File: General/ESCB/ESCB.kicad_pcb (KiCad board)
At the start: 2 copper layers, 35.8 x 17.5 mm, 3 parts, among them J1 Power_Signal, J2 Motor, U1 BESC

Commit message: Update ESCB.kicad_pcb
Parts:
- added G***: LOGO, extraparts:auv_logo, F.Cu at (159.5, 105.8)
- moved J1 21.1 mm to (172.2, 101.2)
- moved U1 21.0 mm to (162.8, 101.2)
- moved J2 20.7 mm to (150.2, 101.2)
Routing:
- net VCC: track 2.54 -> 0.00 mm, vias 10 -> 12
- net Net-(J1-Pad3): track 7.61 -> 8.96 mm
- net Net-(J2-Pad3): vias 3 -> 8
- net Net-(J2-Pad2): vias 3 -> 8
- net Net-(J2-Pad1): vias 3 -> 8
- net GND: vias 10 -> 12
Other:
- board text added: "BESC by Dang Le"
- board text removed: "BESC"

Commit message: Update ESCB.kicad_pcb
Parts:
- moved G*** 1.77 mm to (161.2, 105.5)
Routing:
- net VCC: vias 12 -> 31
- net Net-(J2-Pad3): vias 8 -> 17
- net Net-(J2-Pad2): vias 8 -> 10
- net Net-(J2-Pad1): vias 8 -> 17
- net GND: vias 12 -> 27
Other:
- board size 35.8 x 17.5 mm -> 36 x 17.6 mm

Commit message: Update ESCB.kicad_pcb
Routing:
- net Net-(J1-Pad3): track 8.96 -> 7.97 mm
- net VCC: vias 31 -> 66
- net Net-(J2-Pad3): vias 17 -> 21
- net Net-(J2-Pad1): vias 17 -> 21
- net GND: vias 27 -> 61

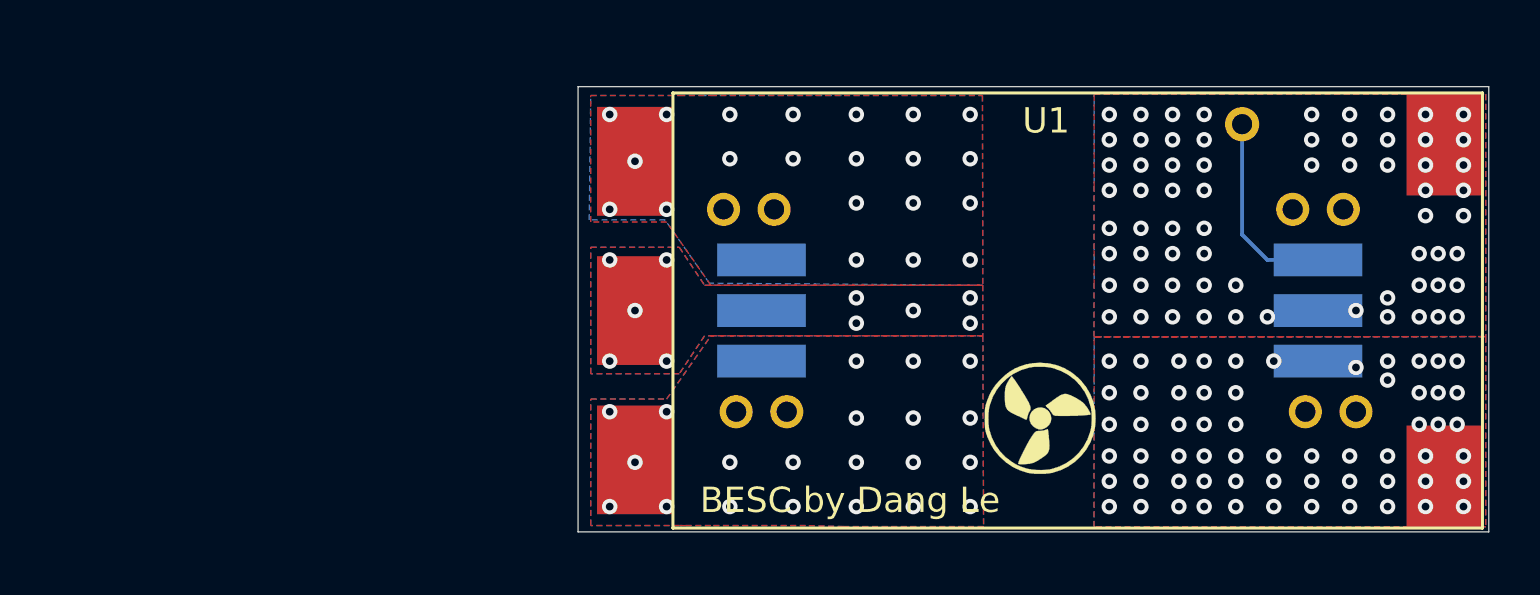
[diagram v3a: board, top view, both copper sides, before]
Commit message: Update Vua and Pore Clearance
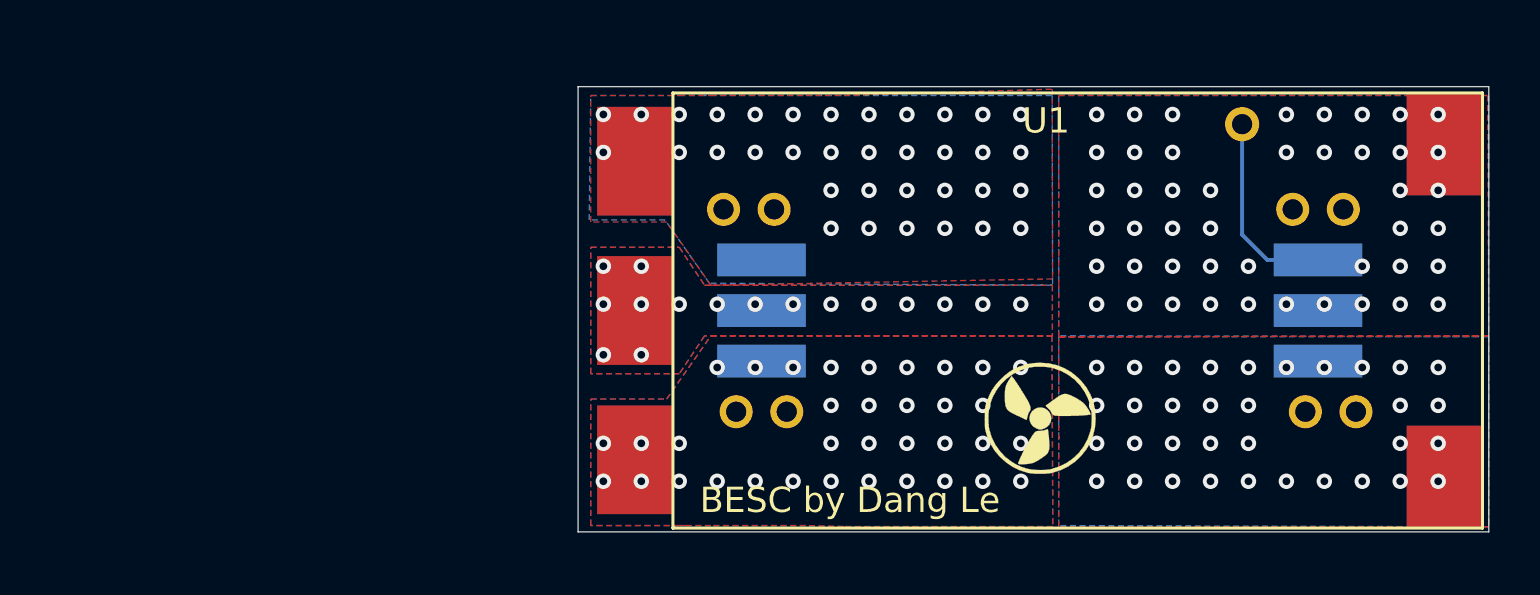
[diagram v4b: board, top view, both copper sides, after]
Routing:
- net Net-(J2-Pad2): track 0.91 -> 0.00 mm, vias 10 -> 16
- net Net-(J1-Pad3): vias 0 -> 1
- net VCC: vias 66 -> 45
- net Net-(J2-Pad3): vias 21 -> 36
- net Net-(J2-Pad1): vias 21 -> 35
- net GND: vias 61 -> 34

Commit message: Used DRC to Correct Pore Errors and Vias overlapping Pads
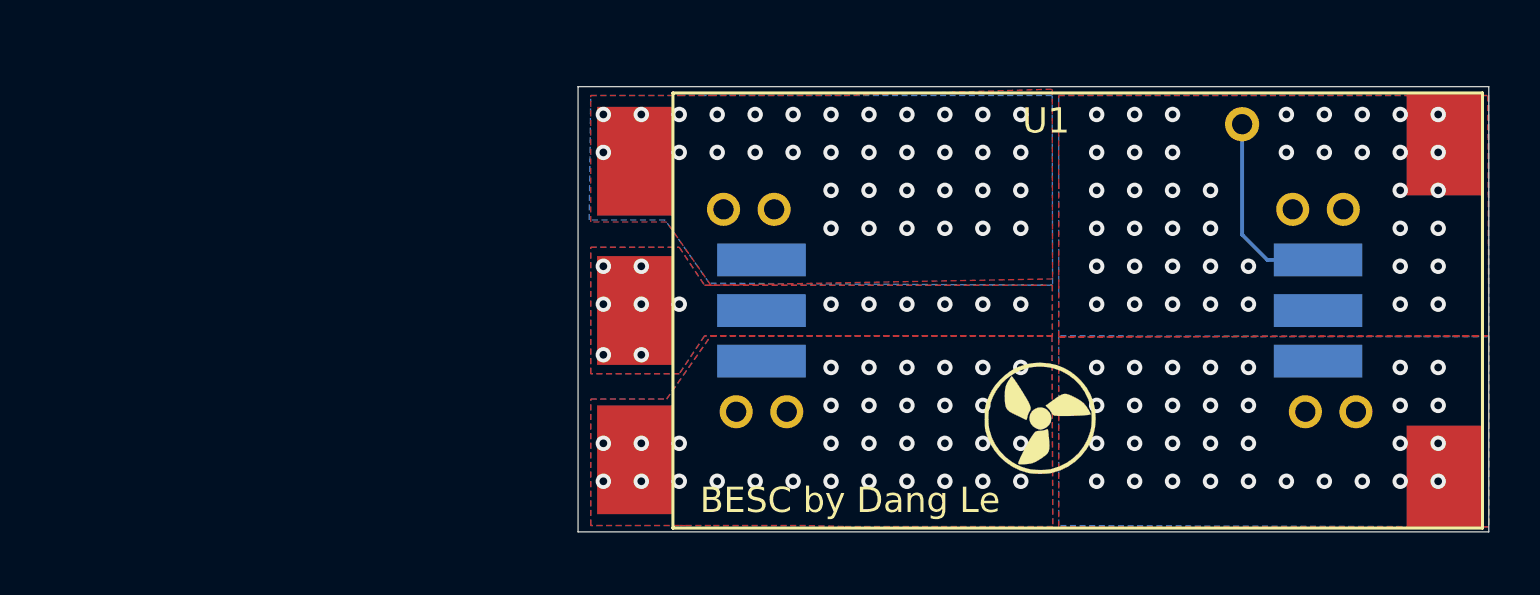
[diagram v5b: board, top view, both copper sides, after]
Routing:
- net VCC: vias 45 -> 42
- net Net-(J2-Pad3): vias 36 -> 33
- net Net-(J2-Pad2): vias 16 -> 13
- net Net-(J1-Pad3): vias 1 -> 0
- net GND: vias 34 -> 31
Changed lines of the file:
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@@
     (thickness 1.6)
     (drawings 5)
-    (tracks 174)
+    (tracks 161)
     (zones 0)
     (modules 4)
@@
   (via (at 144 108) (size 0.6096) (drill 0.3048) (layers F.Cu B.Cu) (net 4))
   (via (at 145.5 108) (size 0.6096) (drill 0.3048) (layers F.Cu B.Cu) (net 4))
-  (via (at 148.5 103.5) (size 0.6096) (drill 0.3048) (layers F.Cu B.Cu) (net 4))
-  (via (at 150 103.5) (size 0.6096) (drill 0.3048) (layers F.Cu B.Cu) (net 4))
-  (via (at 151.5 103.5) (size 0.6096) (drill 0.3048) (layers F.Cu B.Cu) (net 4))
   (via (at 177 108) (size 0.6096) (drill 0.3048) (layers F.Cu B.Cu) (net 3))
   (via (at 177 106.5) (size 0.6096) (drill 0.3048) (layers F.Cu B.Cu) (net 3))
-  (via (at 174 103.5) (size 0.6096) (drill 0.3048) (layers F.Cu B.Cu) (net 3))
-  (via (at 172.5 103.5) (size 0.6096) (drill 0.3048) (layers F.Cu B.Cu) (net 3))
-  (via (at 171 103.5) (size 0.6096) (drill 0.3048) (layers F.Cu B.Cu) (net 3))
   (via (at 145.5 103) (size 0.6096) (drill 0.3048) (layers F.Cu B.Cu) (net 5))
   (via (at 144 103) (size 0.6096) (drill 0.3048) (layers F.Cu B.Cu) (net 5))
@@
   (via (at 144 101) (size 0.6096) (drill 0.3048) (layers F.Cu B.Cu) (net 5))
   (via (at 145.5 101) (size 0.6096) (drill 0.3048) (layers F.Cu B.Cu) (net 5))
-  (via (at 148.5 101) (size 0.6096) (drill 0.3048) (layers F.Cu B.Cu) (net 5))
-  (via (at 150 101) (size 0.6096) (drill 0.3048) (layers F.Cu B.Cu) (net 5))
-  (via (at 151.5 101) (size 0.6096) (drill 0.3048) (layers F.Cu B.Cu) (net 5))
-  (via (at 174 101) (size 0.6096) (drill 0.3048) (layers F.Cu B.Cu) (net 2))
-  (via (at 172.5 101) (size 0.6096) (drill 0.3048) (layers F.Cu B.Cu) (net 2))
-  (via (at 171 101) (size 0.6096) (drill 0.3048) (layers F.Cu B.Cu) (net 2))
-  (via (at 174 99.5) (size 0.6096) (drill 0.3048) (layers F.Cu B.Cu) (net 1))
   (via (at 177 96.5) (size 0.6096) (drill 0.3048) (layers F.Cu B.Cu) (net 2))
   (via (at 177 95) (size 0.6096) (drill 0.3048) (layers F.Cu B.Cu) (net 2))
@@
   )
   (zone (net 3) (net_name GND) (layer F.Cu) (hatch edge 0.508)
+    (priority 3)
     (connect_pads yes (clearance 0.508))
     (min_thickness 0.254)
@@
   )
   (zone (net 2) (net_name VCC) (layer F.Cu) (hatch edge 0.508)
-    (priority 1)
+    (priority 2)
     (connect_pads yes (clearance 0.508))
     (min_thickness 0.254)
@@
   )
   (zone (net 2) (net_name VCC) (layer B.Cu) (hatch edge 0.508)
-    (priority 1)
+    (priority 2)
     (connect_pads yes (clearance 0.508))
     (min_thickness 0.254)
@@
   )
   (zone (net 3) (net_name GND) (layer B.Cu) (hatch edge 0.508)
-    (connect_pads yes (clearance 0.508))
-    (min_thickness 0.254)
-    (fill yes (arc_segments 32) (thermal_gap 0.508) (thermal_bridge_width 0.508))
-    (polygon
-      (pts
-        (xy 179 109.8) (xy 162 109.75) (xy 162 106.26) (xy 162 106.3) (xy 162 105.7)
-        (xy 162 104) (xy 162 102.29) (xy 179 102.28)
-      )
-    )
+    (priority 3)
+    (connect_pads yes (clearance 0.508))
+    (min_thickness 0.254)
+    (fill yes (arc_segments 32) (thermal_gap 0.508) (thermal_bridge_width 0.508))
+    (polygon
+      (pts
+        (xy 179 109.8) (xy 162 109.75) (xy 162 102.29) (xy 179 102.28)
+      )
+    )

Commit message: updated layout
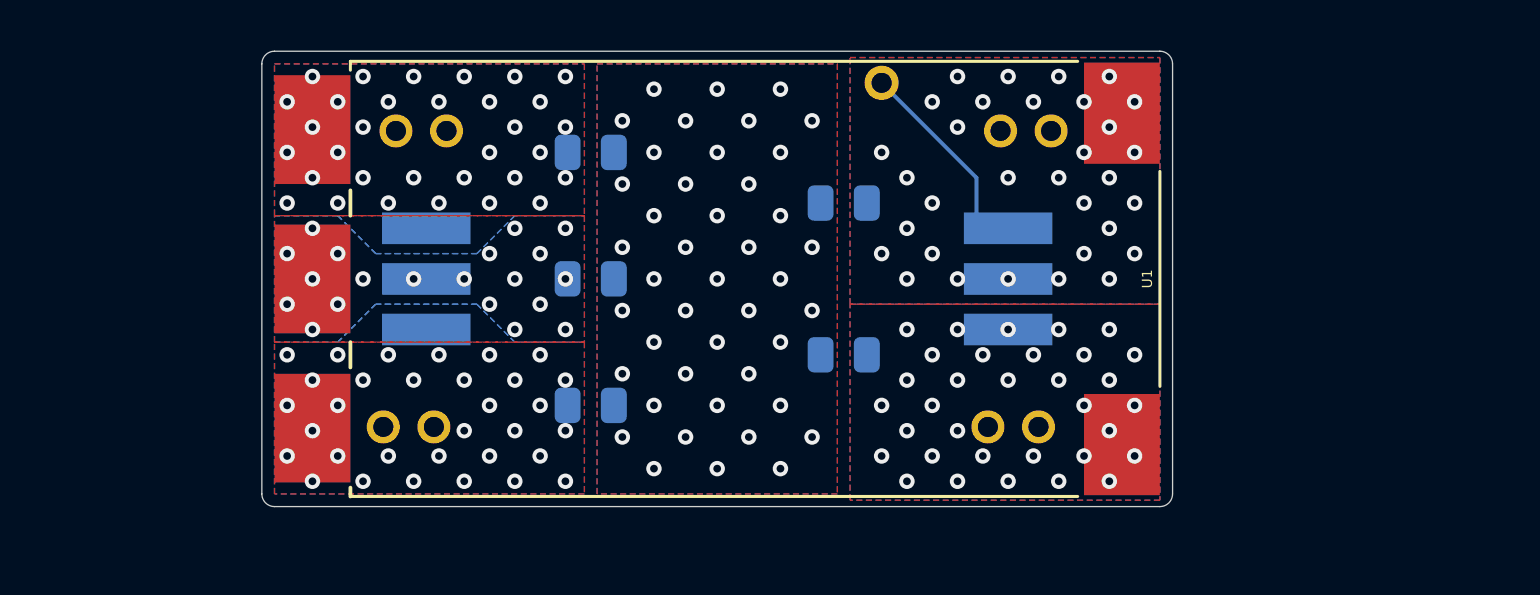
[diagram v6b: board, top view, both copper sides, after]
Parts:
- removed G***: LOGO, extraparts:auv_logo
- added HS1: thermal_jmp, Resistor_SMD:R_0805_2012Metric, B.Cu at (153.5, 97.0)
- added HS2: thermal_jmp, Resistor_SMD:R_0805_2012Metric, B.Cu at (153.5, 103.0)
- added HS3: thermal_jmp, Resistor_SMD:R_0805_2012Metric, B.Cu at (143.5, 95.0)
- added HS4: thermal_jmp, Resistor_SMD:R_0805_2012Metric, B.Cu at (143.5, 100.0)
- added HS5: thermal_jmp, Resistor_SMD:R_0805_2012Metric, B.Cu at (143.5, 105.0)
- J1, J2: footprint extraparts:Samtec_mPOWER_UMPS_3pin -> extraparts:Samtec_mPOWER_UMPT_3pin
- moved J2 13.3 mm to (137.0, 100.0), turned to 90 degrees
- moved U1 12.8 mm to (150.0, 100.0)
- moved J1 12.3 mm to (160.0, 100.0), turned to -90 degrees
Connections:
- net Net-(J1-Pad3) renamed /sig
- J2 pad 1: Net-(J2-Pad1) -> /A
- J2 pad 2: Net-(J2-Pad2) -> /B
- J2 pad 3: Net-(J2-Pad3) -> /C
- U1 pad 4: VCC -> /A
- U1 pad 5: Net-(J2-Pad1) -> /B
- U1 pad 6: Net-(J2-Pad2) -> /C
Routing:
- net Net-(J2-Pad1): track 0.88 -> 0.00 mm, vias 35 -> 0
- net /sig: track 7.97 -> 8.55 mm
- net VCC: vias 42 -> 32
- net Net-(J2-Pad3): vias 33 -> 0
- net Net-(J2-Pad2): vias 13 -> 0
- net GND: vias 31 -> 33
- net /HEAT: vias 0 -> 43
- net /C: vias 0 -> 32
- net /B: vias 0 -> 20
- net /A: vias 0 -> 32
- added copper zone on B.Cu, net /A
- added copper zone on F.Cu, net /A
- added copper zone on B.Cu, net /B
- added copper zone on F.Cu, net /B
- added copper zone on B.Cu, net /C
- added copper zone on F.Cu, net /C
- added copper zone on B.Cu, net /HEAT
- added copper zone on F.Cu, net /HEAT
- removed copper zone on B.Cu, net Net-(J2-Pad1)
- removed copper zone on F.Cu, net Net-(J2-Pad1)
- removed copper zone on B.Cu, net Net-(J2-Pad2)
- removed copper zone on F.Cu, net Net-(J2-Pad2)
- removed copper zone on B.Cu, net Net-(J2-Pad3)
- removed copper zone on F.Cu, net Net-(J2-Pad3)
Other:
- board size 36 x 17.6 mm -> 36 x 18 mm
- net class Default removed
- net class Motor removed
- net class Power removed
- board text added: "ESCB v1 Dang Le Matt Tran"
- board text added: "S + -"
- board text removed: "BESC by Dang Le"
